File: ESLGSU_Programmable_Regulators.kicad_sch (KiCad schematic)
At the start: 94 parts, among them Q1 RE1C002UNTCL, U10 MP28167-A, U11 TPS259474LRPWR, U13 TPS259474LRPWR, U14 MP28167-A, U15 LM73100RPWR, U5 INA219AIDCNR, U9 LM73100RPWR

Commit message: Second last bit of schematic work
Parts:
- removed R10 (x2): 33K, Resistor_SMD:R_0402_1005Metric, symbol Device:R_Small_US
- removed R17 (x2): 10K, Resistor_SMD:R_0402_1005Metric, symbol Device:R_Small_US
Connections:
- net EN_CH1: now also U10.3 (EN); no longer R11.2, R12.1, U11.1 (EN/UVLO), U11.4 (PGTH)
- net EN_CH2: now also U14.3 (EN); no longer R11.2, R12.1, U13.1 (EN/UVLO), U13.4 (PGTH)
- net at U11.3 (PG): no longer U10.3 (EN)
- net at U13.3 (PG): no longer U14.3 (EN)
- new net EN_CH1_EF: R11.2, R12.1, U11.1 (EN/UVLO), U11.4 (PGTH)
- new net EN_CH2_EF: R11.2, R12.1, U13.1 (EN/UVLO), U13.4 (PGTH)
- no-connect marks 2 -> 3
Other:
- note removed: "1.39-4.65V"

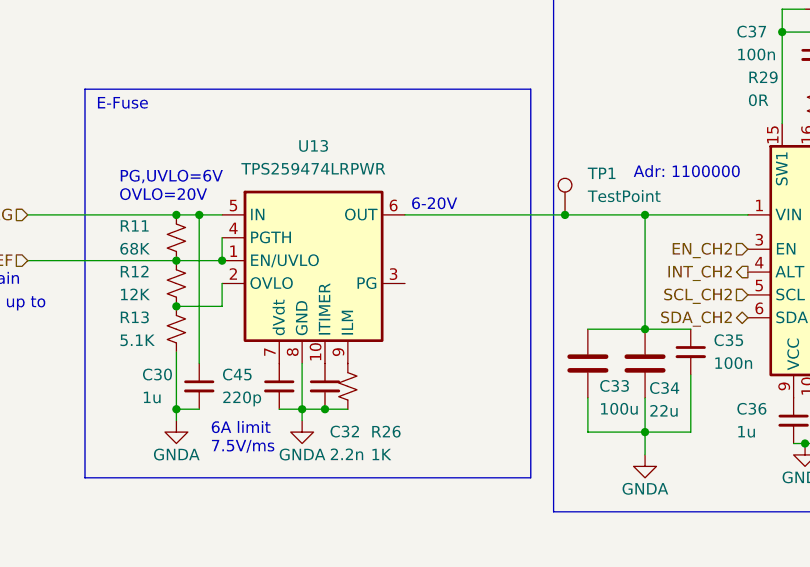
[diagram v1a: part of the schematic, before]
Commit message: Final schematic work, added battery charger, linked everything up
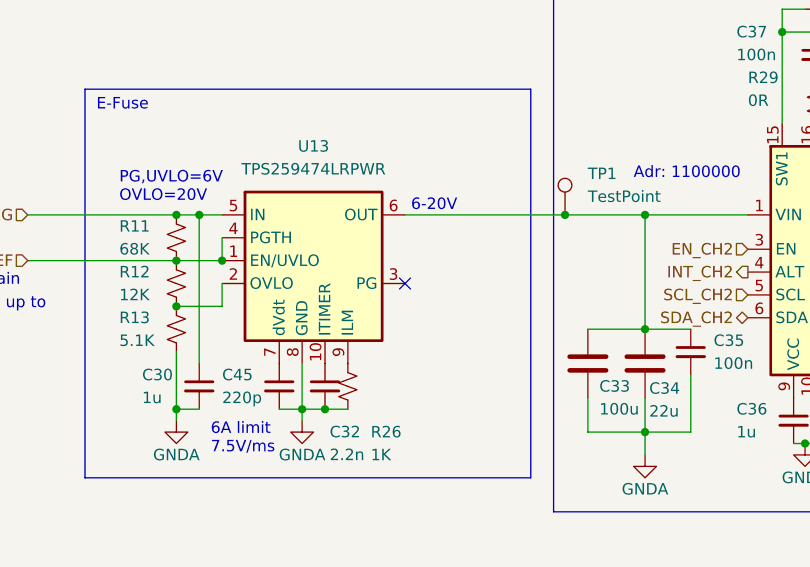
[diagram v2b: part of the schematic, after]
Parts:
- Q1: footprint Package_TO_SOT_SMD:SOT-416 -> Package_TO_SOT_SMD:SOT-23
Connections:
- no-connect marks 3 -> 4
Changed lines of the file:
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@@
   )
   (no_connect (at 200.66 67.31))
+  (no_connect (at 68.58 124.46))
   (no_connect (at 200.66 133.35))
   (no_connect (at 68.58 58.42))
@@
           (reference "R8") (unit 1)
         )
-        (path "/b556fa32-e0cb-409c-ac85-9f2ac606be79/bf0312e4-5726-4684-b2e9-b4b5c1d8e876"
-          (reference "R122") (unit 1)
-        )
         (path "/b556fa32-e0cb-409c-ac85-9f2ac606be79/33c4fea8-f262-455e-abaf-737bb774af6a"
           (reference "R48") (unit 1)
@@
       (effects (font (size 1.27 1.27)) (justify left))
     )
-    (property "Footprint" "Package_TO_SOT_SMD:SOT-416" (at 227.33 126.365 0)
+    (property "Footprint" "Package_TO_SOT_SMD:SOT-23" (at 227.33 126.365 0)
       (effects (font (size 1.27 1.27) italic) (justify left) hide)
     )
@@
       (effects (font (size 1.27 1.27)) (justify left))
     )
-    (property "Footprint" "Package_TO_SOT_SMD:SOT-416" (at 227.33 60.325 0)
+    (property "Footprint" "Package_TO_SOT_SMD:SOT-23" (at 227.33 60.325 0)
       (effects (font (size 1.27 1.27) italic) (justify left) hide)
     )
@@
           (reference "R8") (unit 1)
         )
-        (path "/b556fa32-e0cb-409c-ac85-9f2ac606be79/bf0312e4-5726-4684-b2e9-b4b5c1d8e876"
-          (reference "R122") (unit 1)
-        )
         (path "/b556fa32-e0cb-409c-ac85-9f2ac606be79/33c4fea8-f262-455e-abaf-737bb774af6a"

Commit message: Last tweaks on schematic
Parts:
- removed R11 (x2): 68K, Resistor_SMD:R_0402_1005Metric, symbol Device:R_Small_US
- removed R12 (x2): 12K, Resistor_SMD:R_0402_1005Metric, symbol Device:R_Small_US
- removed R13 (x2): 5.1K, Resistor_SMD:R_0402_1005Metric, symbol Device:R_Small_US
- removed R2 (x2): 5m, Resistor_SMD:R_0603_1608Metric, symbol Device:R_Small_US
- added R14 (x2): 27K, Resistor_SMD:R_0402_1005Metric, symbol Device:R_Small_US
- added R19 (x2): 15K, Resistor_SMD:R_0402_1005Metric, symbol Device:R_Small_US
- added R251 (x2): 8.2K, Resistor_SMD:R_0402_1005Metric, symbol Device:R_Small_US
- added R3 (x2): 5m, Resistor_SMD:R_1206_3216Metric, symbol Device:R_Small_US
- added R9 (x2): 200K, Resistor_SMD:R_0402_1005Metric, symbol Device:R_Small_US
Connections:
- net BUS_CH1: now also R3.1
- net BUS_CH2: now also R3.1
- net BUS_UNREG: now also R9.1, R9.1
- net EN_CH1_EF: now also R14.1, R251.1; no longer U11.1 (EN/UVLO), U11.4 (PGTH)
- net EN_CH2_EF: now also R14.1, R251.1; no longer U13.1 (EN/UVLO), U13.4 (PGTH)
- net GNDA: now also R19.2, R19.2
- net at U11.2 (OVLO): now also R14.2, R19.1
- net at U15.6 (OUT), U5.1 (IN+): now also R3.2
- net at U13.2 (OVLO): now also R14.2, R19.1
- net at U5.1 (IN+), U9.6 (OUT): now also R3.2
- new net: U11.1 (EN/UVLO), U11.4 (PGTH)
- new net: R251.2, R9.2 (x2)
- new net: U13.1 (EN/UVLO), U13.4 (PGTH)
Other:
- note added: "gets pulled up to max 3.3V"
- note removed: "gets pulled up to max 4V"

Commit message: Finished initial revision of PCB
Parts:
- removed Q1 (x2): RE1C002UNTCL, Package_TO_SOT_SMD:SOT-23, symbol Transistor_FET:DMN67D7L
- added Q3 (x2): RE1C002UNTCL, Package_TO_SOT_SMD:SOT-416, symbol Transistor_FET:DMN67D7L
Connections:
- net EN_CH1: no longer U15.1 (EN/UVLO), U15.4 (PGTH)
- net EN_CH2: now also U15.1 (EN/UVLO), U15.4 (PGTH)
- net GND: now also Q3.2 (S), Q3.2 (S)
- net at D1.1 (K): now also Q3.3 (D)
- net at U11.1 (EN/UVLO), U11.4 (PGTH): now also R251.2, R9.2
- net at R87.2, U15.3 (PG): now also Q3.1 (G)
- net at R87.2, U9.3 (PG): now also Q3.1 (G)
- net at D2.1 (K): now also Q3.3 (D)
- net at R251.2, R9.2: now also U13.1 (EN/UVLO), U13.4 (PGTH)
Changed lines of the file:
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@@
   (junction (at 43.18 72.39) (diameter 0) (color 0 0 0 0)
   )
+  (junction (at 190.5 50.8) (diameter 0) (color 0 0 0 0)
+  )
   (junction (at 217.17 124.46) (diameter 0) (color 0 0 0 0)
   )
-  (junction (at 190.5 50.8) (diameter 0) (color 0 0 0 0)
+  (junction (at 43.18 55.88) (diameter 0) (color 0 0 0 0)
   )
   (junction (at 110.49 96.52) (diameter 0) (color 0 0 0 0)
@@
   (junction (at 43.18 138.43) (diameter 0) (color 0 0 0 0)
   )
+  (junction (at 48.26 55.88) (diameter 0) (color 0 0 0 0)
+  )
   (junction (at 229.87 116.84) (diameter 0) (color 0 0 0 0)
   )
@@
   (junction (at 149.86 129.54) (diameter 0) (color 0 0 0 0)
   )
-  (junction (at 217.17 58.42) (diameter 0) (color 0 0 0 0)
-  )
   (junction (at 95.25 129.54) (diameter 0) (color 0 0 0 0)
   )
@@
   (junction (at 190.5 116.84) (diameter 0) (color 0 0 0 0)
   )
+  (junction (at 217.17 58.42) (diameter 0) (color 0 0 0 0)
+  )
   (junction (at 246.38 63.5) (diameter 0) (color 0 0 0 0)
   )
@@
   (junction (at 193.04 121.92) (diameter 0) (color 0 0 0 0)
   )
+  (junction (at 48.26 121.92) (diameter 0) (color 0 0 0 0)
+  )
   (junction (at 130.81 72.39) (diameter 0) (color 0 0 0 0)
   )
@@
   (junction (at 120.65 142.24) (diameter 0) (color 0 0 0 0)
   )
+  (junction (at 43.18 121.92) (diameter 0) (color 0 0 0 0)
+  )
   (junction (at 43.18 60.96) (diameter 0) (color 0 0 0 0)
   )
@@
     (stroke (width 0) (type default))
   )
+  (wire (pts (xy 43.18 121.92) (xy 48.26 121.92))
+    (stroke (width 0) (type default))
+  )
   (wire (pts (xy 229.87 107.95) (xy 232.41 107.95))
     (stroke (width 0) (type default))
@@
     (stroke (width 0) (type default))
   )
+  (wire (pts (xy 43.18 55.88) (xy 48.26 55.88))
+    (stroke (width 0) (type default))
+  )
   (wire (pts (xy 256.54 124.46) (xy 256.54 129.54))
     (stroke (width 0) (type default))
@@
     (effects (font (size 1.27 1.27)) (justify left))
   )
-  (hierarchical_label "EN_CH1" (shape input) (at 191.77 121.92 180) (fields_autoplaced)
+  (hierarchical_label "EN_CH2" (shape input) (at 191.77 121.92 180) (fields_autoplaced)
     (effects (font (size 1.27 1.27)) (justify right))
   )
@@
     )
   )
+  (symbol (lib_id "Transistor_FET:DMN67D7L") (at 222.25 58.42 0) (unit 1)
+    (in_bom yes) (on_board yes) (dnp no)
+    (property "Reference" "Q3" (at 218.44 60.96 0)
+      (effects (font (size 1.27 1.27)) (justify left))
+    )
+    (property "Value" "RE1C002UNTCL" (at 218.44 63.5 0)
+      (effects (font (size 1.27 1.27)) (justify left))
+    )
+    (property "Footprint" "Package_TO_SOT_SMD:SOT-416" (at 227.33 60.325 0)
+      (effects (font (size 1.27 1.27) italic) (justify left) hide)
+    )
+    (property "Datasheet" "http://www.diodes.com/assets/Datasheets/DMN67D7L.pdf" (at 222.25 58.42 0)
+      (effects (font (size 1.27 1.27)) (justify left) hide)
+    )
+    (property "LCSC Part" "C509959" (at 210.82 64.77 0)
+      (effects (font (size 1.27 1.27)) hide)
+    )
+    (pin "1")
+    (pin "2")
+    (pin "3")
+    (instances
+      (project "ESLGSU"
+        (path "/b556fa32-e0cb-409c-ac85-9f2ac606be79/09a64186-e4de-4db7-b903-c6397ff9a54d"
+          (reference "Q3") (unit 1)
+        )
+        (path "/b556fa32-e0cb-409c-ac85-9f2ac606be79/e09c623d-ecce-4ff2-a230-f07fbe15280b"
+          (reference "Q5") (unit 1)
+        )
+        (path "/b556fa32-e0cb-409c-ac85-9f2ac606be79/33c4fea8-f262-455e-abaf-737bb774af6a"
+          (reference "Q5") (unit 1)
+        )
+      )
+    )
+  )
   (symbol (lib_id "Device:C_Small") (at 190.5 69.85 0) (unit 1)
     (in_bom yes) (on_board yes) (dnp no)
@@
     )
   )
-  (symbol (lib_id "Transistor_FET:DMN67D7L") (at 222.25 124.46 0) (unit 1)
-    (in_bom yes) (on_board yes) (dnp no)
-    (property "Reference" "Q1" (at 218.44 127 0)
-      (effects (font (size 1.27 1.27)) (justify left))
-    )
-    (property "Value" "RE1C002UNTCL" (at 218.44 129.54 0)
-      (effects (font (size 1.27 1.27)) (justify left))
-    )
-    (property "Footprint" "Package_TO_SOT_SMD:SOT-23" (at 227.33 126.365 0)
-      (effects (font (size 1.27 1.27) italic) (justify left) hide)
-    )
-    (property "Datasheet" "http://www.diodes.com/assets/Datasheets/DMN67D7L.pdf" (at 222.25 124.46 0)
-      (effects (font (size 1.27 1.27)) (justify left) hide)
-    )
-    (property "LCSC Part" "C509959" (at 210.82 130.81 0)
-      (effects (font (size 1.27 1.27)) hide)
-    )
-    (pin "1")
-    (pin "2")
-    (pin "3")
-    (instances
-      (project "ESLGSU"
-        (path "/b556fa32-e0cb-409c-ac85-9f2ac606be79/09a64186-e4de-4db7-b903-c6397ff9a54d"
-          (reference "Q1") (unit 1)
-        )
-        (path "/b556fa32-e0cb-409c-ac85-9f2ac606be79/e09c623d-ecce-4ff2-a230-f07fbe15280b"
-          (reference "Q5") (unit 1)
-        )
-        (path "/b556fa32-e0cb-409c-ac85-9f2ac606be79/33c4fea8-f262-455e-abaf-737bb774af6a"
-          (reference "Q6") (unit 1)
-        )
-      )
-    )
-  )
   (symbol (lib_id "Device:R_Small_US") (at 102.87 176.53 0) (unit 1)
     (in_bom yes) (on_board yes) (dnp no)
@@
     )
   )
+  (symbol (lib_id "Transistor_FET:DMN67D7L") (at 222.25 124.46 0) (unit 1)
+    (in_bom yes) (on_board yes) (dnp no)
+    (property "Reference" "Q3" (at 218.44 127 0)
+      (effects (font (size 1.27 1.27)) (justify left))
+    )
+    (property "Value" "RE1C002UNTCL" (at 218.44 129.54 0)
+      (effects (font (size 1.27 1.27)) (justify left))
+    )
+    (property "Footprint" "Package_TO_SOT_SMD:SOT-416" (at 227.33 126.365 0)
+      (effects (font (size 1.27 1.27) italic) (justify left) hide)
+    )
+    (property "Datasheet" "http://www.diodes.com/assets/Datasheets/DMN67D7L.pdf" (at 222.25 124.46 0)
+      (effects (font (size 1.27 1.27)) (justify left) hide)
+    )
+    (property "LCSC Part" "C509959" (at 210.82 130.81 0)
+      (effects (font (size 1.27 1.27)) hide)
+    )
+    (pin "1")
+    (pin "2")
+    (pin "3")
+    (instances
+      (project "ESLGSU"
+        (path "/b556fa32-e0cb-409c-ac85-9f2ac606be79/09a64186-e4de-4db7-b903-c6397ff9a54d"
+          (reference "Q3") (unit 1)
+        )
+        (path "/b556fa32-e0cb-409c-ac85-9f2ac606be79/e09c623d-ecce-4ff2-a230-f07fbe15280b"
+          (reference "Q5") (unit 1)
+        )
+        (path "/b556fa32-e0cb-409c-ac85-9f2ac606be79/33c4fea8-f262-455e-abaf-737bb774af6a"
+          (reference "Q6") (unit 1)
+        )
+      )
+    )
+  )
   (symbol (lib_id "Device:C_Small") (at 119.38 33.02 0) (unit 1)
     (in_bom yes) (on_board yes) (dnp no)
@@
         )
       )
-    )
-  )
-  (symbol (lib_id "Transistor_FET:DMN67D7L") (at 222.25 58.42 0) (unit 1)
-    (in_bom yes) (on_board yes) (dnp no)
-    (property "Reference" "Q1" (at 218.44 60.96 0)
-      (effects (font (size 1.27 1.27)) (justify left))
-    )
-    (property "Value" "RE1C002UNTCL" (at 218.44 63.5 0)
-      (effects (font (size 1.27 1.27)) (justify left))
-    )
-    (property "Footprint" "Package_TO_SOT_SMD:SOT-23" (at 227.33 60.325 0)
-      (effects (font (size 1.27 1.27) italic) (justify left) hide)
-    )
-    (property "Datasheet" "http://www.diodes.com/assets/Datasheets/DMN67D7L.pdf" (at 222.25 58.42 0)
-      (effects (font (size 1.27 1.27)) (justify left) hide)
-    )
-    (property "LCSC Part" "C509959" (at 210.82 64.77 0)
-      (effects (font (size 1.27 1.27)) hide)
-    )
-    (pin "1")
-    (pin "2")
-    (pin "3")
-    (instances
-      (project "ESLGSU"
-        (path "/b556fa32-e0cb-409c-ac85-9f2ac606be79/09a64186-e4de-4db7-b903-c6397ff9a54d"
-          (reference "Q1") (unit 1)
-        )
-        (path "/b556fa32-e0cb-409c-ac85-9f2ac606be79/e09c623d-ecce-4ff2-a230-f07fbe15280b"
-          (reference "Q5") (unit 1)
-        )
-        (path "/b556fa32-e0cb-409c-ac85-9f2ac606be79/33c4fea8-f262-455e-abaf-737bb774af6a"
-          (reference "Q5") (unit 1)
-        )
-      )

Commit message: Minimal version
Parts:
- removed C45 (x2): 220p, Capacitor_SMD:C_0402_1005Metric, symbol Device:C_Small
- removed C6 (x2): 100n, Capacitor_SMD:C_0402_1005Metric, symbol Device:C_Small
- removed L1 (x2): SRP1038A-4R7M, Inductor_SMD:L_Vishay_IHLP-4040, symbol Device:L
- removed Q3 (x2): RE1C002UNTCL, Package_TO_SOT_SMD:SOT-416, symbol Transistor_FET:DMN67D7L
- removed R11 (x2): 150K, Resistor_SMD:R_0402_1005Metric, symbol Device:R_Small_US
- removed R11 (x2): 51K, Resistor_SMD:R_0402_1005Metric, symbol Device:R_Small_US
- removed R11 (x2): 220K, Resistor_SMD:R_0402_1005Metric, symbol Device:R_Small_US
- removed R14 (x2): 27K, Resistor_SMD:R_0402_1005Metric, symbol Device:R_Small_US
- removed R15 (x2), R9 (x2): 200K, Resistor_SMD:R_0402_1005Metric, symbol Device:R_Small_US
- removed R19 (x2): 15K, Resistor_SMD:R_0402_1005Metric, symbol Device:R_Small_US
- removed R21 (x2): 22K, Resistor_SMD:R_0402_1005Metric, symbol Device:R_Small_US
- removed R251 (x2): 8.2K, Resistor_SMD:R_0402_1005Metric, symbol Device:R_Small_US
- removed R26 (x2): 1K, Resistor_SMD:R_0402_1005Metric, symbol Device:R_Small_US
- removed R3 (x2): 5m, Resistor_SMD:R_1206_3216Metric, symbol Device:R_Small_US
- removed R8 (x2): 33R, Resistor_SMD:R_0402_1005Metric, symbol Device:R_Small_US
- removed R87 (x2): 47K, Resistor_SMD:R_0402_1005Metric, symbol Device:R_Small_US
- removed TP1 (x6): TestPoint, TestPoint:TestPoint_Pad_D1.5mm, symbol Connector:TestPoint
- removed U5 (x2): INA219AIDCNR, Package_TO_SOT_SMD:SOT-23-8, symbol Sensor_Energy:INA219AxDCN
- added C45 (x2): 220p, Capacitor_SMD:C_0402_1005Metric, symbol Device:C_Small
- added C6 (x2): 100n, Capacitor_SMD:C_0402_1005Metric, symbol Device:C_Small
- added L1 (x2): SRP1038A-4R7M, Inductor_SMD:L_Vishay_IHLP-4040, symbol Device:L
- added Q3 (x2): RE1C002UNTCL, Package_TO_SOT_SMD:SOT-416, symbol Transistor_FET:DMN67D7L
- added R11 (x2): 51K, Resistor_SMD:R_0402_1005Metric, symbol Device:R_Small_US
- added R11 (x2): 220K, Resistor_SMD:R_0402_1005Metric, symbol Device:R_Small_US
- added R11 (x2): 150K, Resistor_SMD:R_0402_1005Metric, symbol Device:R_Small_US
- added R14 (x2): 27K, Resistor_SMD:R_0402_1005Metric, symbol Device:R_Small_US
- added R15 (x2), R9 (x2): 200K, Resistor_SMD:R_0402_1005Metric, symbol Device:R_Small_US
- added R19 (x2): 15K, Resistor_SMD:R_0402_1005Metric, symbol Device:R_Small_US
- added R21 (x2): 22K, Resistor_SMD:R_0402_1005Metric, symbol Device:R_Small_US
- added R251 (x2): 8.2K, Resistor_SMD:R_0402_1005Metric, symbol Device:R_Small_US
- added R26 (x2): 1K, Resistor_SMD:R_0402_1005Metric, symbol Device:R_Small_US
- added R3 (x2): 5m, Resistor_SMD:R_1206_3216Metric, symbol Device:R_Small_US
- added R8 (x2): 33R, Resistor_SMD:R_0402_1005Metric, symbol Device:R_Small_US
- added R87 (x2): 47K, Resistor_SMD:R_0402_1005Metric, symbol Device:R_Small_US
- added TP1 (x6): TestPoint, TestPoint:TestPoint_Pad_D1.5mm, symbol Connector:TestPoint
- added U5 (x2): INA219AIDCNR, Package_TO_SOT_SMD:SOT-23-8, symbol Sensor_Energy:INA219AxDCN
- C12, C13, C14, C15, C17, C18, C19, C20, C21, C22, C23, C24, C25, C26, C27, C28, C30, C32, C33, C34, C35, C36, C37, C38, C39, C40, C41, C42, C43, C44, C45, C46, D1, D2, R29, R30, R4, R5, U10, U11, U13, U14, U15, U9: JLCPCB BOM (none) -> 0; now not fitted; now left out of the parts list
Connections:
- net BUS_CH1: now also R3.1, TP1.1, U5.2 (IN-)
- net BUS_CH2: now also R3.1, TP1.1, U5.2 (IN-)
- net BUS_UNREG: now also R9.1, R9.1
- net EN_CH1_EF: now also R14.1, R251.1
- net EN_CH2_EF: now also R14.1, R251.1
- net GND: now also C6.2, C6.2, Q3.2 (S), Q3.2 (S), U5.3 (GND), U5.3 (GND), U5.7 (A0), U5.7 (A0), U5.8 (A1), U5.8 (A1)
- net GNDA: now also C45.2, C45.2, R11.2, R11.2, R19.2, R19.2, R21.2, R21.2, R26.2, R26.2
- net SCL_CH1: now also U5.5 (SCL)
- net SCL_CH2: now also U5.5 (SCL)
- net SDA_CH1: now also U5.6 (SDA)
- net SDA_CH2: now also U5.6 (SDA)
- net SYS_3V3: now also C6.1, C6.1, R8.1, R8.1, R87.1, R87.1, U5.4 (VS), U5.4 (VS)
- net at C21.1, C22.1, C23.1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: now also R11.1, TP1.1
- net at D1.1 (K): now also Q3.3 (D)
- net at D1.2 (A): now also R8.2
- net at U13.2 (OVLO): now also R14.2, R19.1
- net at U11.1 (EN/UVLO), U11.4 (PGTH): now also R251.2, R9.2
- net at U11.2 (OVLO): now also R14.2, R19.1
- net at C18.1, C19.1, C20.1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: now also TP1.1
- net at U11.7 (dVdt): now also C45.1
- net at U11.9 (ILM): now also R26.1
- net at C40.1, C41.1, C42.1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: now also R11.1, TP1.1
- net at U15.3 (PG): now also Q3.1 (G), R87.2
- net at U15.6 (OUT): now also R3.2, U5.1 (IN+)
- net at U10.8 (FB): now also R15.1
- net at C33.1, C34.1, C35.1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: now also TP1.1
- net at C38.1, U14.14 (SW2): now also L1.2
- net at U9.3 (PG): now also Q3.1 (G), R87.2
- net at C37.1, U14.15 (SW1): now also L1.1
- net at C12.1, U10.15 (SW1): now also L1.1
- net at C13.1, U10.14 (SW2): now also L1.2
- net at C15.1, U10.7 (OC): now also R21.1
- net at U14.8 (FB): now also R15.1
- net at D2.1 (K): now also Q3.3 (D)
- net at D2.2 (A): now also R8.2
- net at U13.9 (ILM): now also R26.1
- net at C39.1, U14.7 (OC): now also R21.1
- net at U13.1 (EN/UVLO), U13.4 (PGTH): now also R251.2, R9.2
- net at U9.6 (OUT): now also R3.2, U5.1 (IN+)
- net at U13.7 (dVdt): now also C45.1
- new net: R11.1, R11.2, R15.2 (x2)
- new net: R11.1, R11.2 (x2)
